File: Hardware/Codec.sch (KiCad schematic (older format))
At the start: 1 part, among them U301 SGTL5000XNAA3

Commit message: Adding some connectivity.
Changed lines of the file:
@@
 Text HLabel 7100 2950 2    50   Output ~ 0
 LineOut_L
+Text HLabel 3100 2700 0    50   Input ~ 0
+i2s_SCLK
+Text HLabel 3100 2800 0    50   Input ~ 0
+i2s_LRCLK
+Text HLabel 7100 3750 2    50   Input ~ 0
+i2s_DOUT
+Text HLabel 3100 3100 0    50   Input ~ 0
+MCLK
+Text HLabel 3100 3300 0    50   Input ~ 0
+i2c1_SCL
+Text HLabel 3100 3400 0    50   Input ~ 0
+i2c1_SDA
+Text HLabel 3100 3000 0    50   Output ~ 0
+i2s_DIN
 $EndSCHEMATC

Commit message: Some passives to codec.
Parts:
- added C? (x3): 1uF, Capacitor_SMD:C_0603_1608Metric, symbol Device:C
- added C? (x2): 0.1uF, Capacitor_SMD:C_0603_1608Metric, symbol Device:C
- added C? (x2): 0.1uF, Capacitor_SMD:C_0603_1608Metric, symbol Device:C_Small
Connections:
- net labels added: HP_VGND
- wire segments 0 -> 7
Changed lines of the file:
@@
 Comment4 ""
 $EndDescr
+Text HLabel 7100 2850 2    50   Output ~ 0
+LineOut_R
+Text HLabel 7100 2950 2    50   Output ~ 0
+LineOut_L
+Text HLabel 4350 3650 0    50   Input ~ 0
+i2s_SCLK
+Text HLabel 4350 3550 0    50   Input ~ 0
+i2s_LRCLK
+Text HLabel 7100 3550 2    50   Input ~ 0
+i2s_DOUT
+Text HLabel 4350 3450 0    50   Input ~ 0
+MCLK
+Text HLabel 4350 4050 0    50   Input ~ 0
+i2c1_SCL
+Text HLabel 4350 3950 0    50   Input ~ 0
+i2c1_SDA
+Text HLabel 4350 3750 0    50   Output ~ 0
+i2s_DIN
+$Comp
+L Device:C C?
+U 1 1 6137DB9E
+P 2350 4850
+AR Path="/611E335F/6137DB9E" Ref="C?"  Part="1"
+AR Path="/611E3218/611E32E1/6137DB9E" Ref="C?"  Part="1"
+F 0 "C?" H 2465 5032 50  0000 L CNN
+F 1 "1uF" H 2465 4941 50  0000 L CNN
+F 2 "Capacitor_SMD:C_0603_1608Metric" H 2388 4700 50  0001 C CNN
+F 3 "~" H 2350 4850 50  0001 C CNN
+F 4 "GMK107AB7105KAHT" H 2350 4850 50  0001 C CNN "MPN"
+F 5 "587-3352-1-ND" H 2350 4850 50  0001 C CNN "DPN"
+F 6 "35V" H 2465 4850 50  0000 L CNN "Tol"
+F 7 "0603" H 2465 4759 50  0000 L CNN "Pkg"
+F 8 "X7R" H 2465 4668 50  0000 L CNN "TCoff"
+	1    2350 4850
+	1    0    0    -1
+$EndComp
+$Comp
+L Device:C C?
+U 1 1 6137E467
+P 2900 5600
+AR Path="/611E335F/6137E467" Ref="C?"  Part="1"
+AR Path="/611E3218/611E32E1/6137E467" Ref="C?"  Part="1"
+F 0 "C?" H 3015 5782 50  0000 L CNN
+F 1 "0.1uF" H 3015 5691 50  0000 L CNN
+F 2 "Capacitor_SMD:C_0603_1608Metric" H 2938 5450 50  0001 C CNN
+F 3 "~" H 2900 5600 50  0001 C CNN
+F 4 "C0603C104K5RACAUTO" H 2900 5600 50  0001 C CNN "MPN"
+F 5 "399-6856-1-ND" H 2900 5600 50  0001 C CNN "DPN"
+F 6 "50V" H 3015 5600 50  0000 L CNN "Tol"
+F 7 "0603" H 3015 5509 50  0000 L CNN "Pkg"
+F 8 "X7R" H 3015 5418 50  0000 L CNN "TCoff"
+	1    2900 5600
+	1    0    0    -1
+$EndComp
+$Comp
+L Device:C C?
+U 1 1 6137E472
+P 2350 5600
+AR Path="/611E335F/6137E472" Ref="C?"  Part="1"
+AR Path="/611E3218/611E32E1/6137E472" Ref="C?"  Part="1"
+F 0 "C?" H 2465 5782 50  0000 L CNN
+F 1 "1uF" H 2465 5691 50  0000 L CNN
+F 2 "Capacitor_SMD:C_0603_1608Metric" H 2388 5450 50  0001 C CNN
+F 3 "~" H 2350 5600 50  0001 C CNN
+F 4 "GMK107AB7105KAHT" H 2350 5600 50  0001 C CNN "MPN"
+F 5 "587-3352-1-ND" H 2350 5600 50  0001 C CNN "DPN"
+F 6 "35V" H 2465 5600 50  0000 L CNN "Tol"
+F 7 "0603" H 2465 5509 50  0000 L CNN "Pkg"
+F 8 "X7R" H 2465 5418 50  0000 L CNN "TCoff"
+	1    2350 5600
+	1    0    0    -1
+$EndComp
+$Comp
+L Device:C C?
+U 1 1 6137E7B9
+P 2100 3150
+AR Path="/611E335F/6137E7B9" Ref="C?"  Part="1"
+AR Path="/611E3218/611E32E1/6137E7B9" Ref="C?"  Part="1"
+F 0 "C?" H 2215 3332 50  0000 L CNN
+F 1 "0.1uF" H 2215 3241 50  0000 L CNN
+F 2 "Capacitor_SMD:C_0603_1608Metric" H 2138 3000 50  0001 C CNN
+F 3 "~" H 2100 3150 50  0001 C CNN
+F 4 "C0603C104K5RACAUTO" H 2100 3150 50  0001 C CNN "MPN"
+F 5 "399-6856-1-ND" H 2100 3150 50  0001 C CNN "DPN"
+F 6 "50V" H 2215 3150 50  0000 L CNN "Tol"
+F 7 "0603" H 2215 3059 50  0000 L CNN "Pkg"
+F 8 "X7R" H 2215 2968 50  0000 L CNN "TCoff"
+	1    2100 3150
+	0    1    1    0
+$EndComp
+Text Label 6150 3350 0    50   ~ 0
+HP_VGND
+Wire Wire Line
+	6150 4350 6050 4350
+$Comp
+L Device:C_Small C?
+U 1 1 61383D31
+P 6250 4100
+AR Path="/611E335F/61383D31" Ref="C?"  Part="1"
+AR Path="/611E3218/611E32E1/61383D31" Ref="C?"  Part="1"
+F 0 "C?" H 6365 4282 50  0000 L CNN
+F 1 "0.1uF" H 6365 4191 50  0000 L CNN
+F 2 "Capacitor_SMD:C_0603_1608Metric" H 6288 3950 50  0001 C CNN
+F 3 "~" H 6250 4100 50  0001 C CNN
+F 4 "C0603C104K5RACAUTO" H 6250 4100 50  0001 C CNN "MPN"
+F 5 "399-6856-1-ND" H 6250 4100 50  0001 C CNN "DPN"
+F 6 "50V" H 6365 4100 50  0000 L CNN "Tol"
+F 7 "0603" H 6365 4009 50  0000 L CNN "Pkg"
+F 8 "X7R" H 6365 3918 50  0000 L CNN "TCoff"
+	1    6250 4100
+	1    0    0    -1
+$EndComp
+Wire Wire Line
+	4350 3950 4450 3950
+Wire Wire Line
+	4350 4050 4450 4050
+Wire Wire Line
+	4350 3750 4450 3750
+Wire Wire Line
+	4350 3650 4450 3650
+Wire Wire Line
+	4350 3550 4450 3550
+Wire Wire Line
+	4350 3450 4450 3450
 $Comp
 L SGTL5000XNAA:SGTL5000XNAA3 U301
@@
 	1    0    0    -1
 $EndComp
-Text HLabel 7100 2850 2    50   Output ~ 0
-LineOut_R
-Text HLabel 7100 2950 2    50   Output ~ 0
-LineOut_L
-Text HLabel 3100 2700 0    50   Input ~ 0
-i2s_SCLK
-Text HLabel 3100 2800 0    50   Input ~ 0
-i2s_LRCLK
-Text HLabel 7100 3750 2    50   Input ~ 0
-i2s_DOUT
-Text HLabel 3100 3100 0    50   Input ~ 0
-MCLK
-Text HLabel 3100 3300 0    50   Input ~ 0
-i2c1_SCL
-Text HLabel 3100 3400 0    50   Input ~ 0
-i2c1_SDA
-Text HLabel 3100 3000 0    50   Output ~ 0
-i2s_DIN
+$Comp
+L Device:C_Small C?
+U 1 1 61393087
+P 6700 4100
+AR Path="/611E335F/61393087" Ref="C?"  Part="1"
+AR Path="/611E3218/611E32E1/61393087" Ref="C?"  Part="1"
+F 0 "C?" H 6815 4282 50  0000 L CNN
+F 1 "0.1uF" H 6815 4191 50  0000 L CNN
+F 2 "Capacitor_SMD:C_0603_1608Metric" H 6738 3950 50  0001 C CNN
+F 3 "~" H 6700 4100 50  0001 C CNN
+F 4 "C0603C104K5RACAUTO" H 6700 4100 50  0001 C CNN "MPN"
+F 5 "399-6856-1-ND" H 6700 4100 50  0001 C CNN "DPN"
+F 6 "50V" H 6815 4100 50  0000 L CNN "Tol"
+F 7 "0603" H 6815 4009 50  0000 L CNN "Pkg"
+F 8 "X7R" H 6815 3918 50  0000 L CNN "TCoff"
+	1    6700 4100
+	1    0    0    -1
+$EndComp
+$Comp
+L Device:C C?
+U 1 1 61395780
+P 2750 3450
+AR Path="/611E335F/61395780" Ref="C?"  Part="1"
+AR Path="/611E3218/611E32E1/61395780" Ref="C?"  Part="1"
+F 0 "C?" H 2865 3632 50  0000 L CNN
+F 1 "1uF" H 2865 3541 50  0000 L CNN
+F 2 "Capacitor_SMD:C_0603_1608Metric" H 2788 3300 50  0001 C CNN
+F 3 "~" H 2750 3450 50  0001 C CNN
+F 4 "GMK107AB7105KAHT" H 2750 3450 50  0001 C CNN "MPN"
+F 5 "587-3352-1-ND" H 2750 3450 50  0001 C CNN "DPN"
+F 6 "35V" H 2865 3450 50  0000 L CNN "Tol"
+F 7 "0603" H 2865 3359 50  0000 L CNN "Pkg"
+F 8 "X7R" H 2865 3268 50  0000 L CNN "TCoff"
+	1    2750 3450
+	1    0    0    -1
+$EndComp
 $EndSCHEMATC

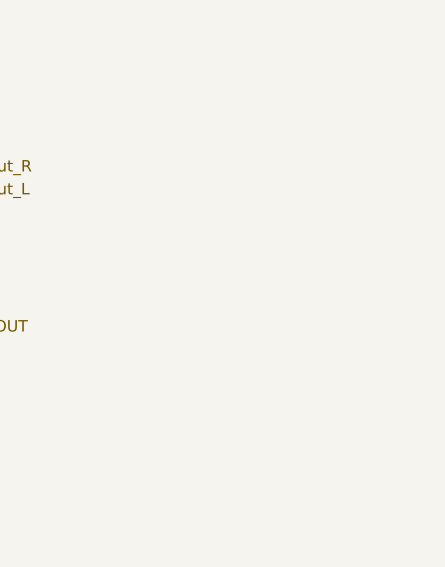
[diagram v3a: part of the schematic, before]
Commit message: Power connectivity going in.
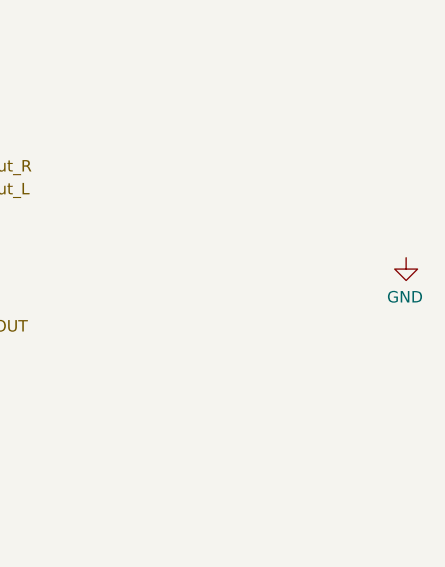
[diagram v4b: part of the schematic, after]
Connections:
- net labels added: GND
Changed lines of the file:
@@
 	1    0    0    -1
 $EndComp
+$Comp
+L power:GND #PWR?
+U 1 1 613B1DC0
+P 9150 3250
+F 0 "#PWR?" H 9150 3000 50  0001 C CNN
+F 1 "GND" H 9155 3077 50  0000 C CNN
+F 2 "" H 9150 3250 50  0001 C CNN
+F 3 "" H 9150 3250 50  0001 C CNN
+	1    9150 3250
+	-1   0    0    -1
+$EndComp
 $EndSCHEMATC

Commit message: Putting in some connectivity. More passives.
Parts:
- added C308, C309: 1uF, Capacitor_SMD:C_0603_1608Metric, symbol Device:C
- added R301: R, symbol Device:R
- gave numbers to parts that had none: 7
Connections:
- net labels added: +3V3, HP_L, HP_R, MIC_IN
- wire segments 7 -> 22
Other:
- moved on the sheet: C304
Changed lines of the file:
@@
 Comment4 ""
 $EndDescr
-Text HLabel 7100 2850 2    50   Output ~ 0
+Text HLabel 7700 2850 2    50   Output ~ 0
 LineOut_R
-Text HLabel 7100 2950 2    50   Output ~ 0
+Text HLabel 7700 2950 2    50   Output ~ 0
 LineOut_L
 Text HLabel 4350 3650 0    50   Input ~ 0
@@
 Text HLabel 4350 3550 0    50   Input ~ 0
 i2s_LRCLK
-Text HLabel 7100 3550 2    50   Input ~ 0
+Text HLabel 7700 3550 2    50   Input ~ 0
 i2s_DOUT
 Text HLabel 4350 3450 0    50   Input ~ 0
@@
 P 2350 4850
 AR Path="/611E335F/6137DB9E" Ref="C?"  Part="1"
-AR Path="/611E3218/611E32E1/6137DB9E" Ref="C?"  Part="1"
-F 0 "C?" H 2465 5032 50  0000 L CNN
+AR Path="/611E3218/611E32E1/6137DB9E" Ref="C302"  Part="1"
+F 0 "C302" H 2465 5032 50  0000 L CNN
 F 1 "1uF" H 2465 4941 50  0000 L CNN
 F 2 "Capacitor_SMD:C_0603_1608Metric" H 2388 4700 50  0001 C CNN
@@
 P 2900 5600
 AR Path="/611E335F/6137E467" Ref="C?"  Part="1"
-AR Path="/611E3218/611E32E1/6137E467" Ref="C?"  Part="1"
-F 0 "C?" H 3015 5782 50  0000 L CNN
+AR Path="/611E3218/611E32E1/6137E467" Ref="C305"  Part="1"
+F 0 "C305" H 3015 5782 50  0000 L CNN
 F 1 "0.1uF" H 3015 5691 50  0000 L CNN
 F 2 "Capacitor_SMD:C_0603_1608Metric" H 2938 5450 50  0001 C CNN
@@
 P 2350 5600
 AR Path="/611E335F/6137E472" Ref="C?"  Part="1"
-AR Path="/611E3218/611E32E1/6137E472" Ref="C?"  Part="1"
-F 0 "C?" H 2465 5782 50  0000 L CNN
+AR Path="/611E3218/611E32E1/6137E472" Ref="C303"  Part="1"
+F 0 "C303" H 2465 5782 50  0000 L CNN
 F 1 "1uF" H 2465 5691 50  0000 L CNN
 F 2 "Capacitor_SMD:C_0603_1608Metric" H 2388 5450 50  0001 C CNN
@@
 P 2100 3150
 AR Path="/611E335F/6137E7B9" Ref="C?"  Part="1"
-AR Path="/611E3218/611E32E1/6137E7B9" Ref="C?"  Part="1"
-F 0 "C?" H 2215 3332 50  0000 L CNN
+AR Path="/611E3218/611E32E1/6137E7B9" Ref="C301"  Part="1"
+F 0 "C301" H 2215 3332 50  0000 L CNN
 F 1 "0.1uF" H 2215 3241 50  0000 L CNN
 F 2 "Capacitor_SMD:C_0603_1608Metric" H 2138 3000 50  0001 C CNN
@@
 P 6250 4100
 AR Path="/611E335F/61383D31" Ref="C?"  Part="1"
-AR Path="/611E3218/611E32E1/61383D31" Ref="C?"  Part="1"
-F 0 "C?" H 6365 4282 50  0000 L CNN
+AR Path="/611E3218/611E32E1/61383D31" Ref="C306"  Part="1"
+F 0 "C306" H 6365 4282 50  0000 L CNN
 F 1 "0.1uF" H 6365 4191 50  0000 L CNN
 F 2 "Capacitor_SMD:C_0603_1608Metric" H 6288 3950 50  0001 C CNN
@@
 P 6700 4100
 AR Path="/611E335F/61393087" Ref="C?"  Part="1"
-AR Path="/611E3218/611E32E1/61393087" Ref="C?"  Part="1"
-F 0 "C?" H 6815 4282 50  0000 L CNN
+AR Path="/611E3218/611E32E1/61393087" Ref="C307"  Part="1"
+F 0 "C307" H 6815 4282 50  0000 L CNN
 F 1 "0.1uF" H 6815 4191 50  0000 L CNN
 F 2 "Capacitor_SMD:C_0603_1608Metric" H 6738 3950 50  0001 C CNN
@@
 L Device:C C?
 U 1 1 61395780
-P 2750 3450
+P 2800 3600
 AR Path="/611E335F/61395780" Ref="C?"  Part="1"
-AR Path="/611E3218/611E32E1/61395780" Ref="C?"  Part="1"
-F 0 "C?" H 2865 3632 50  0000 L CNN
-F 1 "1uF" H 2865 3541 50  0000 L CNN
-F 2 "Capacitor_SMD:C_0603_1608Metric" H 2788 3300 50  0001 C CNN
-F 3 "~" H 2750 3450 50  0001 C CNN
-F 4 "GMK107AB7105KAHT" H 2750 3450 50  0001 C CNN "MPN"
-F 5 "587-3352-1-ND" H 2750 3450 50  0001 C CNN "DPN"
-F 6 "35V" H 2865 3450 50  0000 L CNN "Tol"
-F 7 "0603" H 2865 3359 50  0000 L CNN "Pkg"
-F 8 "X7R" H 2865 3268 50  0000 L CNN "TCoff"
-	1    2750 3450
+AR Path="/611E3218/611E32E1/61395780" Ref="C304"  Part="1"
+F 0 "C304" H 2915 3782 50  0000 L CNN
+F 1 "1uF" H 2915 3691 50  0000 L CNN
+F 2 "Capacitor_SMD:C_0603_1608Metric" H 2838 3450 50  0001 C CNN
+F 3 "~" H 2800 3600 50  0001 C CNN
+F 4 "GMK107AB7105KAHT" H 2800 3600 50  0001 C CNN "MPN"
+F 5 "587-3352-1-ND" H 2800 3600 50  0001 C CNN "DPN"
+F 6 "35V" H 2915 3600 50  0000 L CNN "Tol"
+F 7 "0603" H 2915 3509 50  0000 L CNN "Pkg"
+F 8 "X7R" H 2915 3418 50  0000 L CNN "TCoff"
+	1    2800 3600
 	1    0    0    -1
 $EndComp
@@
 L power:GND #PWR?
 U 1 1 613B1DC0
-P 9150 3250
-F 0 "#PWR?" H 9150 3000 50  0001 C CNN
-F 1 "GND" H 9155 3077 50  0000 C CNN
-F 2 "" H 9150 3250 50  0001 C CNN
-F 3 "" H 9150 3250 50  0001 C CNN
-	1    9150 3250
+P 6150 4600
+AR Path="/611E3335/613B1DC0" Ref="#PWR?"  Part="1"
+AR Path="/611E3218/611E32E1/613B1DC0" Ref="#PWR0106"  Part="1"
+F 0 "#PWR0106" H 6150 4350 50  0001 C CNN
+F 1 "GND" H 6155 4427 50  0000 C CNN
+F 2 "" H 6150 4600 50  0001 C CNN
+F 3 "" H 6150 4600 50  0001 C CNN
+	1    6150 4600
 	-1   0    0    -1
 $EndComp
+$Comp
+L Device:R R301
+U 1 1 6144AA4D
+P 2600 3250
+F 0 "R301" V 2807 3250 50  0000 C CNN
+F 1 "R" V 2716 3250 50  0000 C CNN
+F 2 "" V 2530 3250 50  0001 C CNN
+F 3 "~" H 2600 3250 50  0001 C CNN
+	1    2600 3250
+	0    -1   -1   0
+$EndComp
+$Comp
+L Device:C C?
+U 1 1 61454CD6
+P 7250 2850
+AR Path="/611E335F/61454CD6" Ref="C?"  Part="1"
+AR Path="/611E3218/611E32E1/61454CD6" Ref="C309"  Part="1"
+F 0 "C309" H 7365 3032 50  0000 L CNN
+F 1 "1uF" H 7365 2941 50  0000 L CNN
+F 2 "Capacitor_SMD:C_0603_1608Metric" H 7288 2700 50  0001 C CNN
+F 3 "~" H 7250 2850 50  0001 C CNN
+F 4 "GMK107AB7105KAHT" H 7250 2850 50  0001 C CNN "MPN"
+F 5 "587-3352-1-ND" H 7250 2850 50  0001 C CNN "DPN"
+F 6 "35V" H 7365 2850 50  0000 L CNN "Tol"
+F 7 "0603" H 7365 2759 50  0000 L CNN "Pkg"
+F 8 "X7R" H 7365 2668 50  0000 L CNN "TCoff"
+	1    7250 2850
+	0    -1   -1   0
+$EndComp
+$Comp
+L Device:C C?
+U 1 1 61454CE1
+P 6850 2950
+AR Path="/611E335F/61454CE1" Ref="C?"  Part="1"
+AR Path="/611E3218/611E32E1/61454CE1" Ref="C308"  Part="1"
+AR Path="/611E3218/611E330D/61454CE1" Ref="C?"  Part="1"
+F 0 "C308" H 6965 3132 50  0000 L CNN
+F 1 "1uF" H 6965 3041 50  0000 L CNN
+F 2 "Capacitor_SMD:C_0603_1608Metric" H 6888 2800 50  0001 C CNN
+F 3 "~" H 6850 2950 50  0001 C CNN
+F 4 "GMK107AB7105KAHT" H 6850 2950 50  0001 C CNN "MPN"
+F 5 "587-3352-1-ND" H 6850 2950 50  0001 C CNN "DPN"
+F 6 "35V" H 6965 2950 50  0000 L CNN "Tol"
+F 7 "0603" H 6965 2859 50  0000 L CNN "Pkg"
+F 8 "X7R" H 6965 2768 50  0000 L CNN "TCoff"
+	1    6850 2950
+	0    -1   1    0
+$EndComp
+Wire Wire Line
+	6050 2850 7100 2850
+Wire Wire Line
+	7400 2850 7700 2850
+Wire Wire Line
+	6050 2950 6700 2950
+Wire Wire Line
+	7000 2950 7700 2950
+$Comp
+L power:+3V3 #PWR?
+U 1 1 6145BB5A
+P 6200 2050
+AR Path="/6123BB15/6145BB5A" Ref="#PWR?"  Part="1"
+AR Path="/611E335F/6145BB5A" Ref="#PWR?"  Part="1"
+AR Path="/611E3218/611E32E1/6145BB5A" Ref="#PWR0123"  Part="1"
+F 0 "#PWR0123" H 6200 1900 50  0001 C CNN
+F 1 "+3V3" H 6215 2223 50  0000 C CNN
+F 2 "" H 6200 2050 50  0001 C CNN
+F 3 "" H 6200 2050 50  0001 C CNN
+	1    6200 2050
+	1    0    0    -1
+$EndComp
+Wire Wire Line
+	6200 2050 6200 2350
+Wire Wire Line
+	6050 2350 6200 2350
+Wire Wire Line
+	6050 2450 6200 2450
+Wire Wire Line
+	6200 2450 6200 2350
+Connection ~ 6200 2350
+Wire Wire Line
+	6050 2550 6200 2550
+Wire Wire Line
+	6200 2550 6200 2450
+Connection ~ 6200 2450
+Wire Wire Line
+	6050 3550 7700 3550
+Wire Wire Line
+	6050 3750 6700 3750
+Wire Wire Line
+	6700 3750 6700 4000
+Wire Wire Line
+	6100 3950 6250 3950
+Wire Wire Line
+	6250 3950 6250 4000
+Text HLabel 1850 3150 0    50   Input ~ 0
+MIC_IN
+Text HLabel 7700 3150 2    50   Input ~ 0
+HP_R
+Text HLabel 7700 3250 2    50   Input ~ 0
+HP_L
+Text HLabel 7700 3350 2    50   Input ~ 0
+HP_VGND
 $EndSCHEMATC

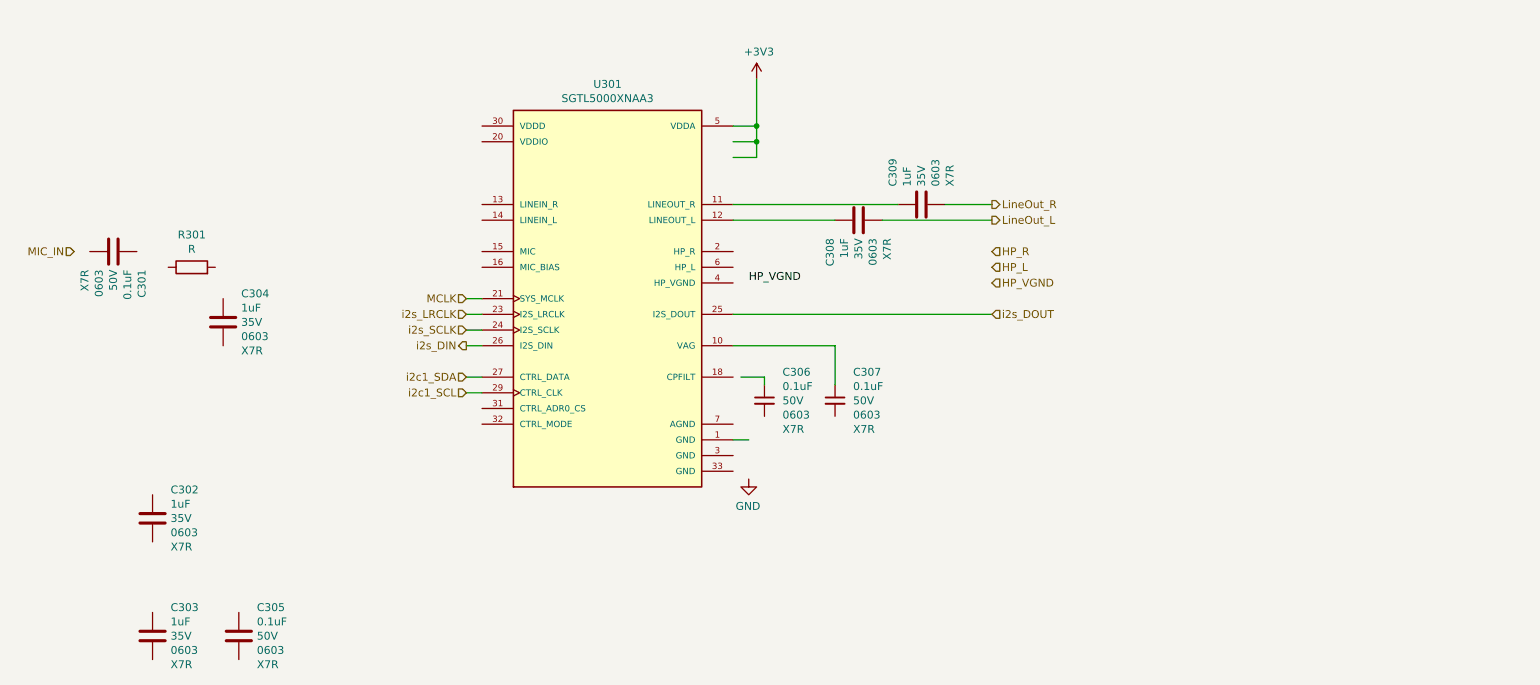
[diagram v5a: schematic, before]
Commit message: More passives.
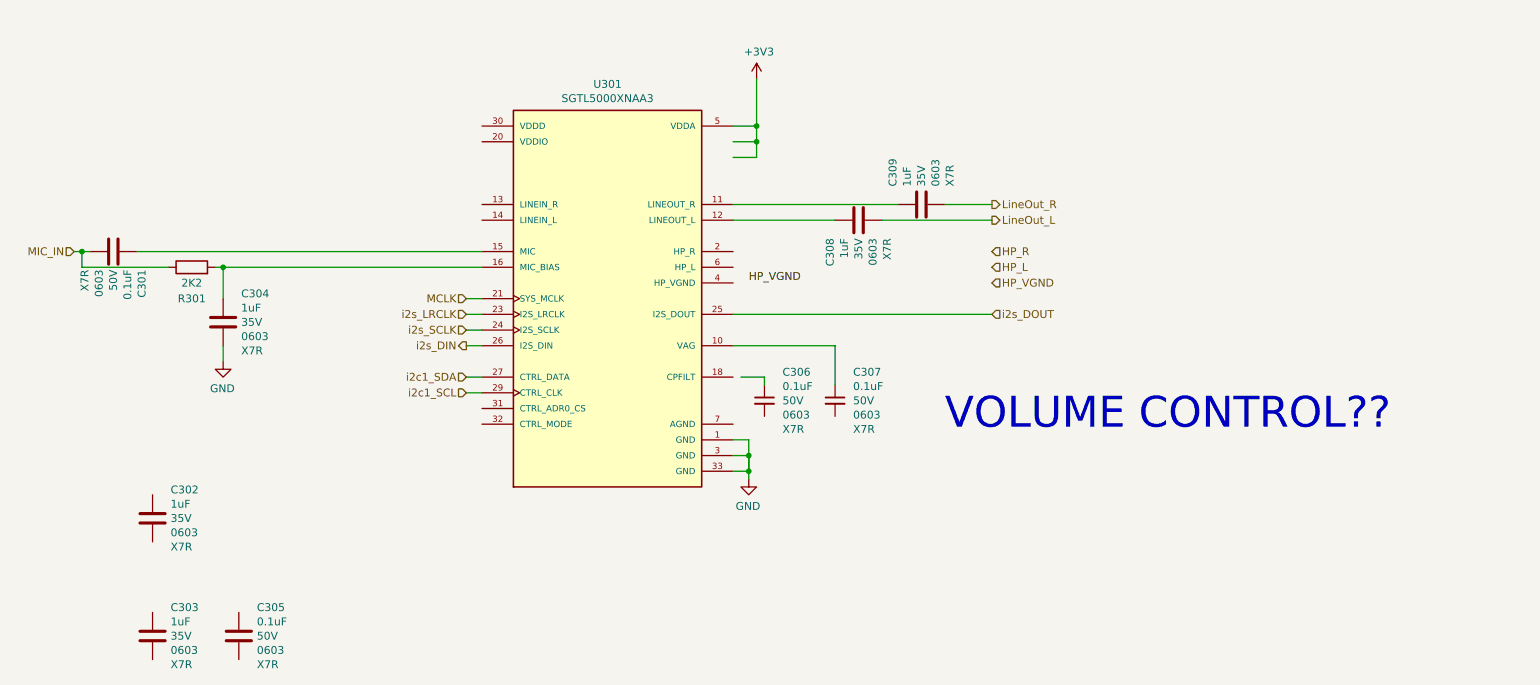
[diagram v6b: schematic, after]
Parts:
- R301: value R -> 2K2; footprint (none) -> Resistor_SMD:R_0603_1608Metric
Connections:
- wire segments 22 -> 37
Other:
- note added: "VOLUME CONTROL??"
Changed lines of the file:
@@
 U 1 1 6144AA4D
 P 2600 3250
-F 0 "R301" V 2807 3250 50  0000 C CNN
-F 1 "R" V 2716 3250 50  0000 C CNN
-F 2 "" V 2530 3250 50  0001 C CNN
+F 0 "R301" V 2400 3250 50  0000 C CNN
+F 1 "2K2" V 2500 3250 50  0000 C CNN
+F 2 "Resistor_SMD:R_0603_1608Metric" V 2530 3250 50  0001 C CNN
 F 3 "~" H 2600 3250 50  0001 C CNN
 	1    2600 3250
@@
 Text HLabel 7700 3350 2    50   Input ~ 0
 HP_VGND
+Wire Wire Line
+	4450 3250 2800 3250
+Wire Wire Line
+	2800 3450 2800 3250
+Connection ~ 2800 3250
+Wire Wire Line
+	2800 3250 2750 3250
+Wire Wire Line
+	4450 3150 2250 3150
+Wire Wire Line
+	2450 3250 1900 3250
+Wire Wire Line
+	1900 3250 1900 3150
+Wire Wire Line
+	1900 3150 1950 3150
+Wire Wire Line
+	1850 3150 1900 3150
+Connection ~ 1900 3150
+$Comp
+L power:GND #PWR?
+U 1 1 6152EDEA
+P 2800 3850
+AR Path="/611E3335/6152EDEA" Ref="#PWR?"  Part="1"
+AR Path="/611E3218/611E32E1/6152EDEA" Ref="#PWR?"  Part="1"
+F 0 "#PWR?" H 2800 3600 50  0001 C CNN
+F 1 "GND" H 2805 3677 50  0000 C CNN
+F 2 "" H 2800 3850 50  0001 C CNN
+F 3 "" H 2800 3850 50  0001 C CNN
+	1    2800 3850
+	-1   0    0    -1
+$EndComp
+Wire Wire Line
+	2800 3750 2800 3850
+Wire Wire Line
+	6150 4600 6150 4550
+Wire Wire Line
+	6150 4550 6050 4550
+Wire Wire Line
+	6050 4450 6150 4450
+Wire Wire Line
+	6150 4450 6150 4550
+Connection ~ 6150 4550
+Wire Wire Line
+	6150 4350 6150 4450
+Connection ~ 6150 4450
+Wire Wire Line
+	6150 4450 6150 4550
+Text Notes 7400 4300 0    197  ~ 0
+VOLUME CONTROL??
 $EndSCHEMATC
